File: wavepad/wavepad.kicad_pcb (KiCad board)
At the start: 2 copper layers, 18 parts, among them SW1 SW_Push, SW2 SW_Push, SW3 SW_Push, SW4 SW_Push, SW5 SW_Push, SW6 SW_Push, SW7 SW_Push, SW8 SW_Push, U1 Seeed Studio XIAO SAMD21

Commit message: actually finish design
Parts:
- moved D1 86.7 mm to (173.6, 43.7), turned to -90 degrees
- moved D2 83.8 mm to (169.6, 43.7), turned to -90 degrees
- moved D3 81.4 mm to (166.1, 43.7), turned to -90 degrees
- moved D4 79.2 mm to (162.5, 43.7), turned to -90 degrees
- moved D5 77.4 mm to (158.9, 43.7), turned to -90 degrees
- moved D6 75.9 mm to (155.6, 43.7), turned to -90 degrees
- moved D7 74.6 mm to (152.1, 43.7), turned to -90 degrees
- moved D8 69.5 mm to (148.6, 43.7), turned to -90 degrees
- moved Brd1 15.0 mm to (121.1, 26.6)
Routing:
- net Net-(D5-A): track 12.4 -> 176.7 mm
- net Net-(D6-A): track 32.0 -> 135.4 mm
- net Row 1: track 24.6 -> 106.9 mm
- net Net-(D2-A): track 90.8 -> 12.6 mm
- net Net-(D8-A): track 0.00 -> 62.1 mm
- net Net-(D7-A): track 53.6 -> 102.6 mm
- net Net-(D4-A): track 15.1 -> 61.7 mm
- net Row 2: track 39.6 -> 84.5 mm
- net SCL: track 87.3 -> 125.7 mm
- net SDA: track 93.1 -> 118.3 mm
- net Net-(D1-A): track 52.7 -> 36.5 mm
- net Net-(D3-A): track 34.6 -> 46.5 mm
- net +3.3V: track 64.0 -> 74.6 mm
- net GND: track 68.1 -> 64.8 mm
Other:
- board outline added: 90 x 75 mm

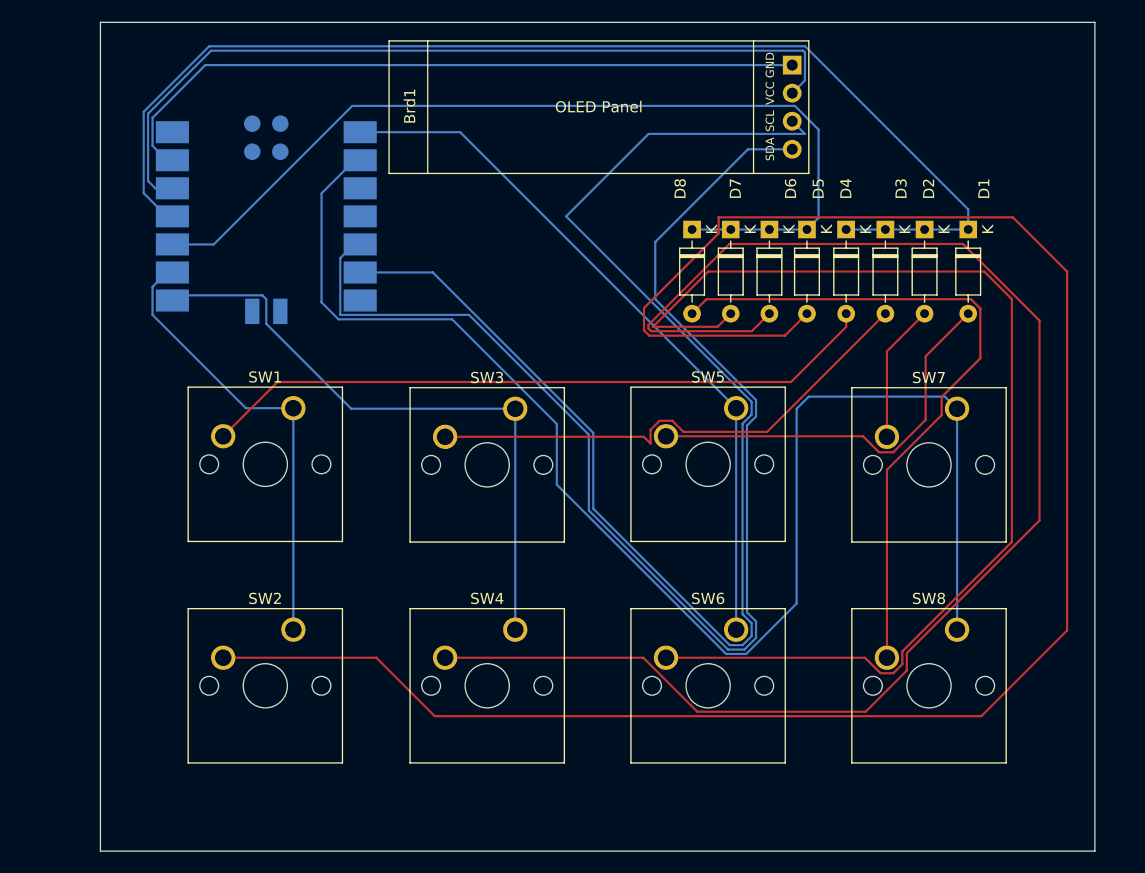
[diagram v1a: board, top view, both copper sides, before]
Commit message: add resistors to oled
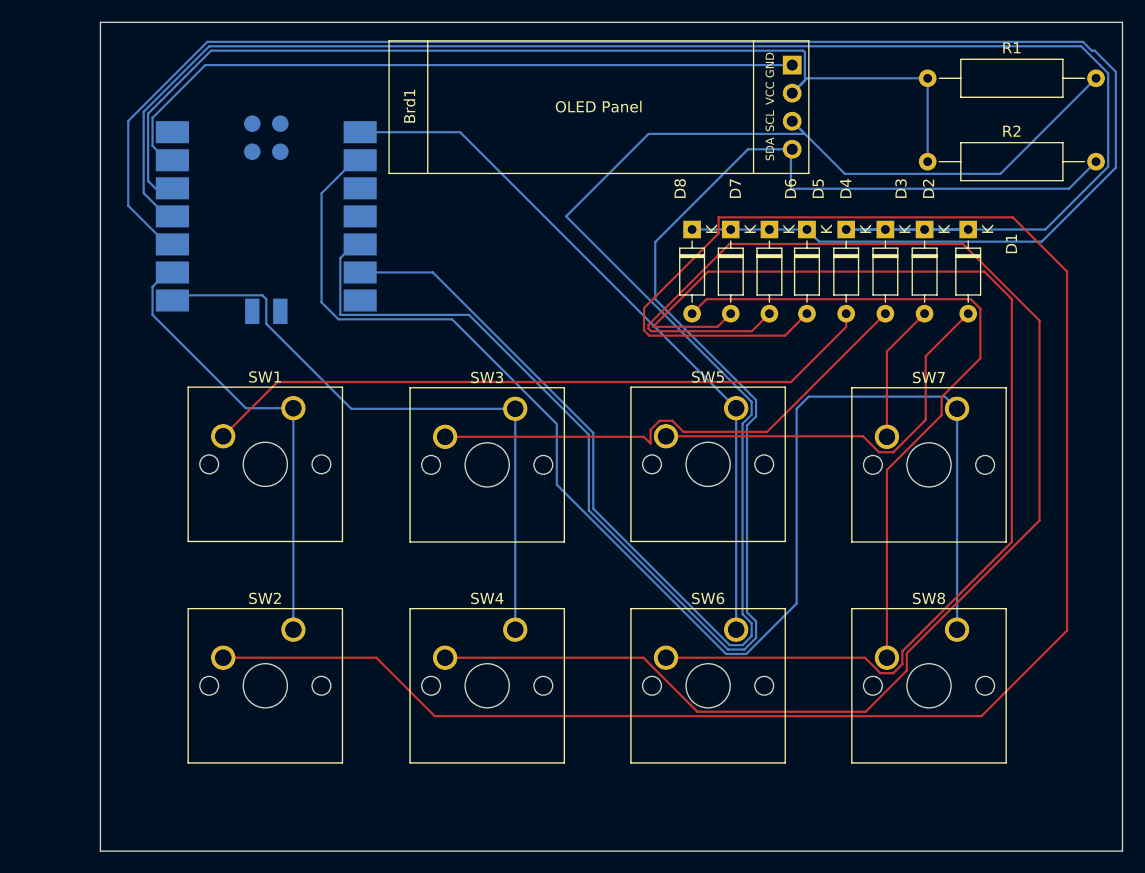
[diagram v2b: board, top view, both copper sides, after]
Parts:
- added R1: R, Resistor_THT:R_Axial_DIN0309_L9.0mm_D3.2mm_P15.24mm_Horizontal, F.Cu at (169.9, 30.0)
- added R2: R, Resistor_THT:R_Axial_DIN0309_L9.0mm_D3.2mm_P15.24mm_Horizontal, F.Cu at (169.9, 37.5)
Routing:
- net Row 2: track 84.5 -> 156.9 mm
- net Row 1: track 106.9 -> 147.2 mm
- net SCL: track 125.7 -> 158.8 mm
- net SDA: track 118.3 -> 150.5 mm
- net +3.3V: track 74.6 -> 95.0 mm
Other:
- board size 90 x 75 mm -> 92.5 x 75 mm
